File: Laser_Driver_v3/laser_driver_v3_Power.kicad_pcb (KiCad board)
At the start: 2 copper layers, 261.3 x 165.2 mm, 178 parts, among them J1 Screw_Terminal_01x03, J2 Screw_Terminal_01x03, J3 Screw_Terminal_01x03, J4 Screw_Terminal_01x03, J5 Screw_Terminal_01x03, J6 Conn_02x12_Counter_Clockwise, Q1 IRF540NPBF, Q10 Q_NPN MJL21194, Q2 IRF9540NPBF, Q3 IRF540NPBF, Q4 IRF9540NPBF, Q5 MMBT2907, Q6 MMBT2222, Q7 Q_PNP_MJL21193, Q8 Q_PNP_MJL21193, Q9 Q_NPN MJL21194, U1 MC7808CTG, U10 LT3042EMSE +14.3V, U11 LM4041A, U12 LM4041, U13 MC7812CTG, U14 MC7808CTG, U15 LT3045EMSE 5V, U16 LT3045EMSE 5V, U17 MC7808CTG, U18 LM7905_TO220, U19 LT3045EMSE 5V, U2 LT3042EMSE +5.5V, U20 LT3094EMSE -5V, U21 OPA192IDBVR, U3 LTC6655BHMS8-5#PBF, U4 MC7812CTG, U5 MC7805CTG, U6 LT3045EMSE 3.3V, U7 LP5907MFX-1.8, U8 TPS7A3901DSCR, U9 LT3094EMSE -14.3V

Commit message: Update zeners to LM4051 SOT-23
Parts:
- R25: moved to F.Cu
- U11: value LM4041A -> LM4051AIM3-ADJ/NOPB; footprint Package_TO_SOT_THT:TO-92_Inline -> Package_TO_SOT_SMD:SOT-23_Handsoldering
- U12: value LM4041 -> LM4051AIM3-ADJ/NOPB; footprint Package_TO_SOT_THT:TO-92_Inline -> Package_TO_SOT_SMD:SOT-23_Handsoldering
- moved R31 7.77 mm to (88.2, 109.8), turned to 0 degrees
- moved R30 4.62 mm to (85.2, 105.4), turned to -90 degrees
- moved R24 2.83 mm to (52.4, 109.2)
- moved R25 2.72 mm to (49.4, 106.0)
- moved U11 2.57 mm to (52.2, 105.5)
- moved U12 2.46 mm to (88.0, 105.9)
- moved C29 0.69 mm to (215.4, 52.0)
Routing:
- net DGND: track 498.0 -> 503.1 mm, vias 4 -> 3
- net Net-(U12-FB): track 7.51 -> 4.76 mm
- net Net-(D10-K): track 8.02 -> 5.46 mm
- net Net-(D11-A): track 7.88 -> 5.41 mm
- net Net-(U8-OUTN): track 60.1 -> 58.3 mm
- net Net-(U11-FB): track 5.89 -> 4.14 mm

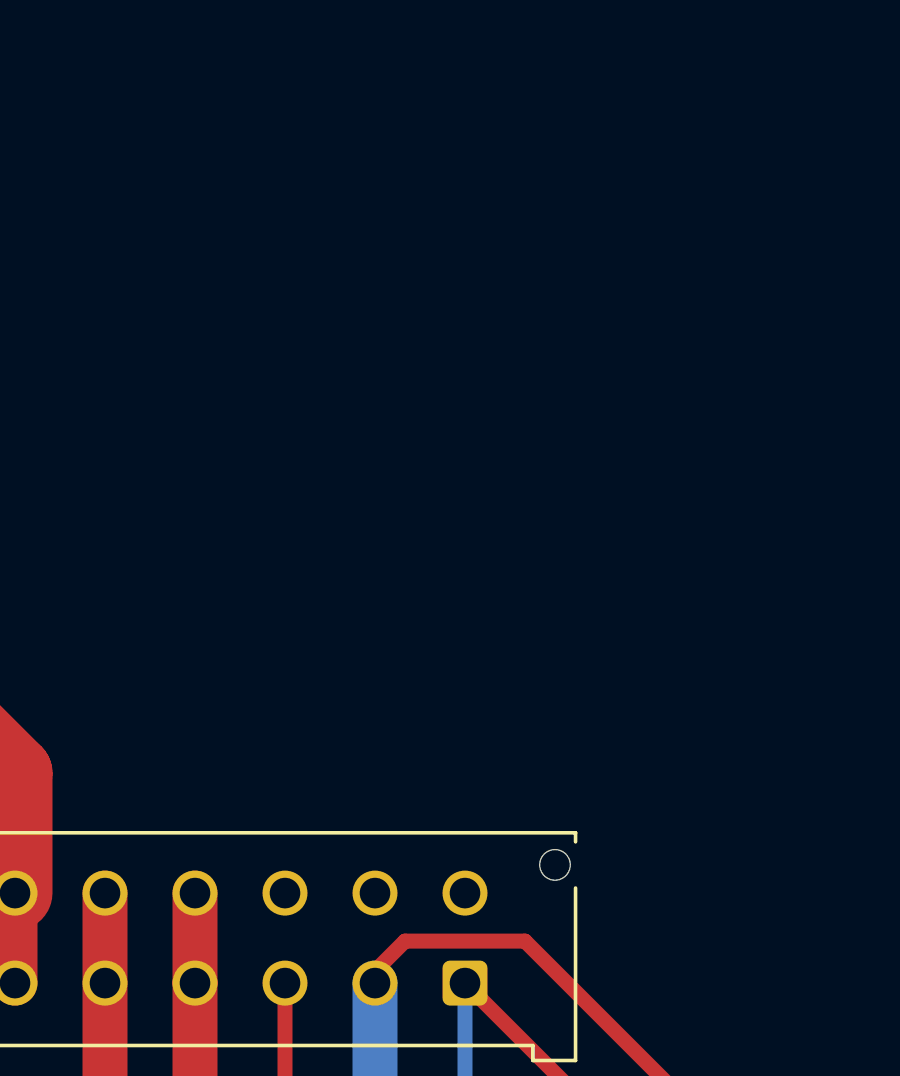
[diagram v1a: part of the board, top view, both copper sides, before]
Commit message: Added NTC for heatsink.  orrected screw terminal#s
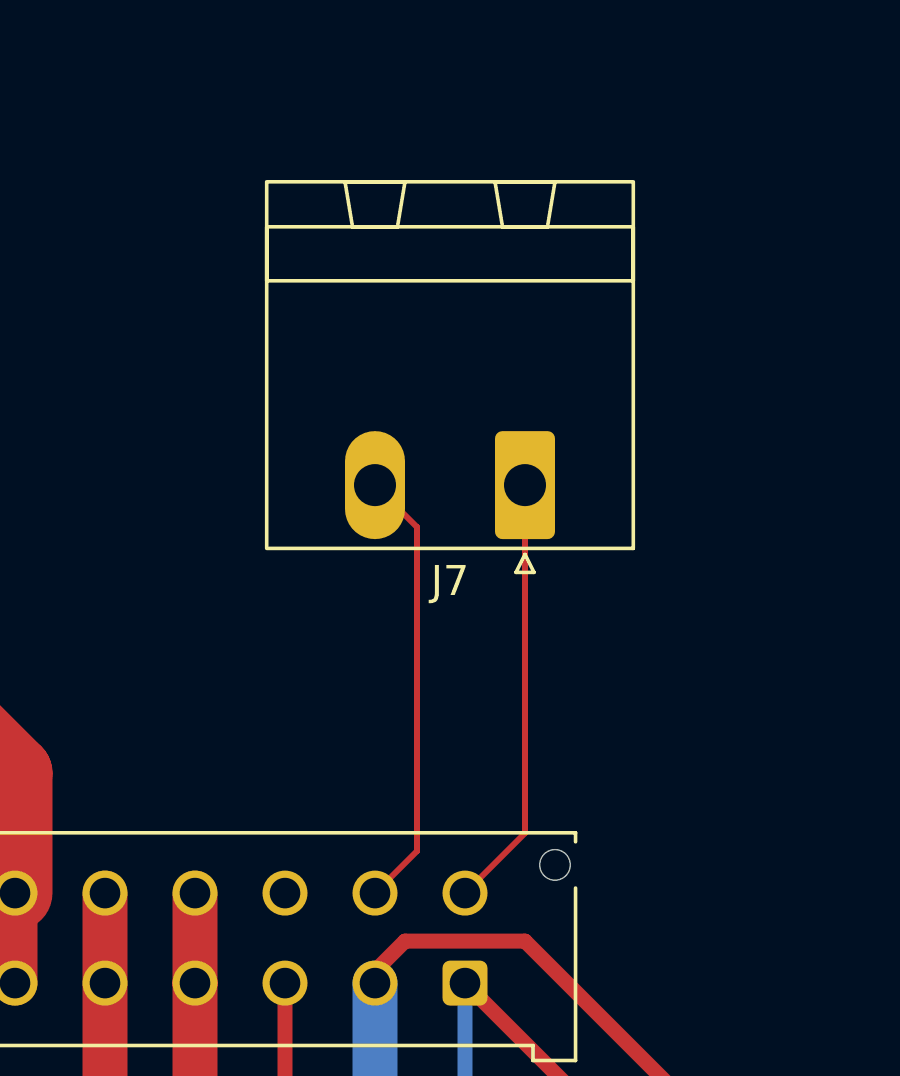
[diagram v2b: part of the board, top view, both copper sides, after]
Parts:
- added J7: Conn_01x02_Pin, Connector_Phoenix_MSTB:PhoenixContact_MSTBA_2,5_2-G_1x02_P5.00mm_Horizontal, F.Cu at (261.6, 33.8)
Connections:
- J6 pad 13: GND -> Net-(J6-Pin_13)
- J6 pad 14: GND -> Net-(J6-Pin_14)
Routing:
- net Net-(J6-Pin_14): track 0.00 -> 14.8 mm
- net Net-(J6-Pin_13): track 0.00 -> 14.4 mm

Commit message: Adding rail voltage good led circuitry.
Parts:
- added H1: MountingHole, MountingHole:MountingHole_3.2mm_M3, F.Cu at (22.6, 36.6)
- added H2: MountingHole, MountingHole:MountingHole_3.2mm_M3, F.Cu at (23.8, 170.4)
- added H3: MountingHole, MountingHole:MountingHole_3.2mm_M3, F.Cu at (142.6, 47.8)
- added H4: MountingHole, MountingHole:MountingHole_3.2mm_M3, F.Cu at (153.8, 121.0)
- added H5: MountingHole, MountingHole:MountingHole_3.2mm_M3, F.Cu at (271.0, 17.2)
- added H6: MountingHole, MountingHole:MountingHole_3.2mm_M3, F.Cu at (270.0, 170.4)
- added H7: GND, MountingHole:MountingHole_3.2mm_M3_DIN965_Pad_TopBottom, F.Cu at (108.0, 25.0)
- moved R3 14.1 mm to (183.0, 170.2)
- moved R20 14.1 mm to (79.1, 170.0)
- moved R2 14.1 mm to (234.6, 170.4)
- moved R21 14.1 mm to (130.2, 170.4)
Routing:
- net /Mains to +-18V/RAW22+: track 108.8 -> 126.7 mm
- net Net-(D8-K): track 188.8 -> 174.3 mm
- net Earth: track 14.1 -> 24.4 mm
- net /Mains to +-18V/-22VNF: track 172.8 -> 164.3 mm
- net /+-6V TEC/TEC_RAW+: track 233.1 -> 241.5 mm
- net /+-6V TEC/TEC_RAW-: track 313.9 -> 307.7 mm
- net /Mains to +-18V/RAW22-: track 103.1 -> 106.7 mm
- net Net-(J2-Pin_3): track 134.7 -> 132.0 mm
- net Net-(D9-A): track 141.9 -> 139.6 mm
- net /Mains to +-18V/+22VNF: track 136.4 -> 137.8 mm

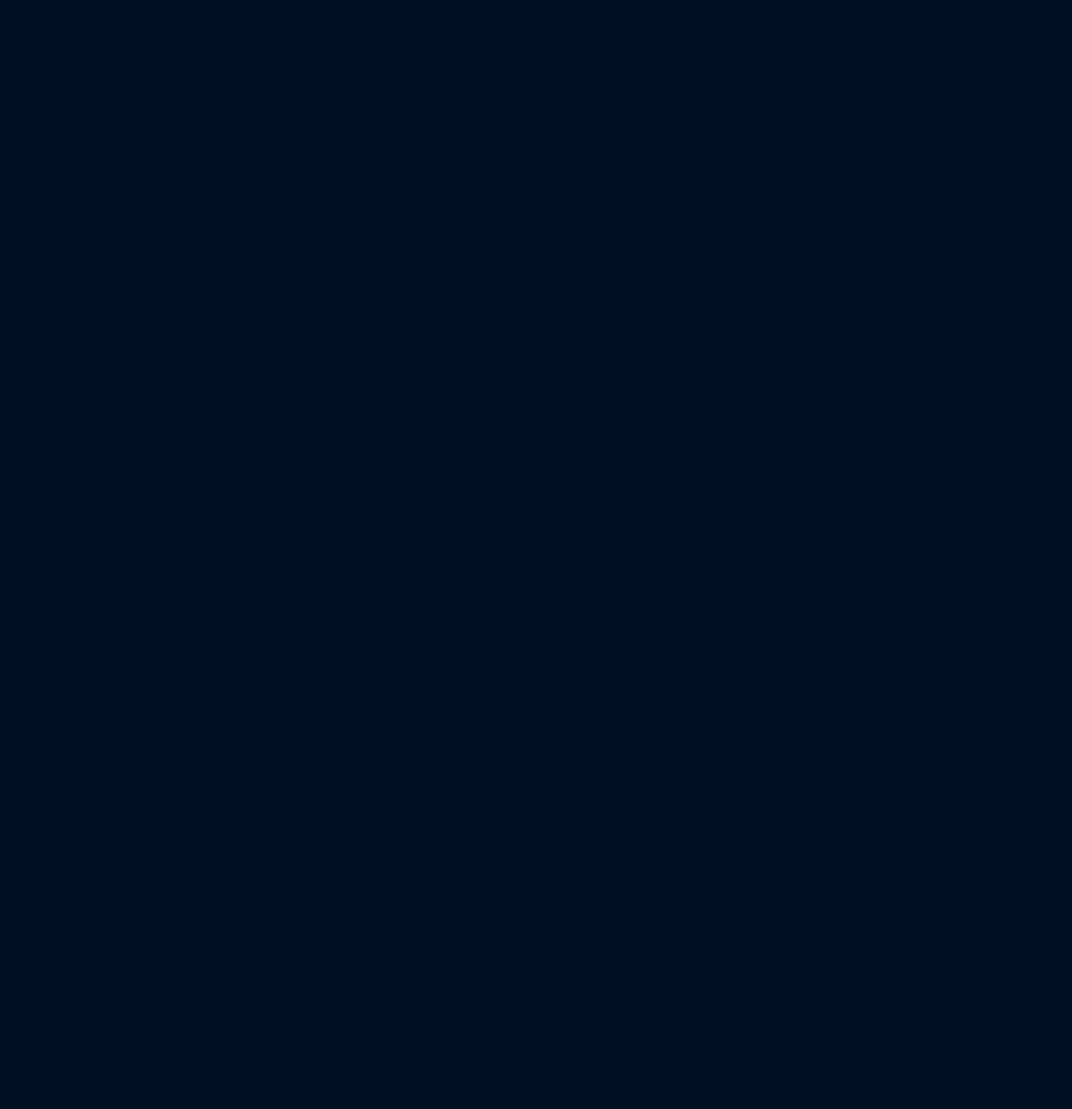
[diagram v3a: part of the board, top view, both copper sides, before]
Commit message: Started placing voltage monitor parts.
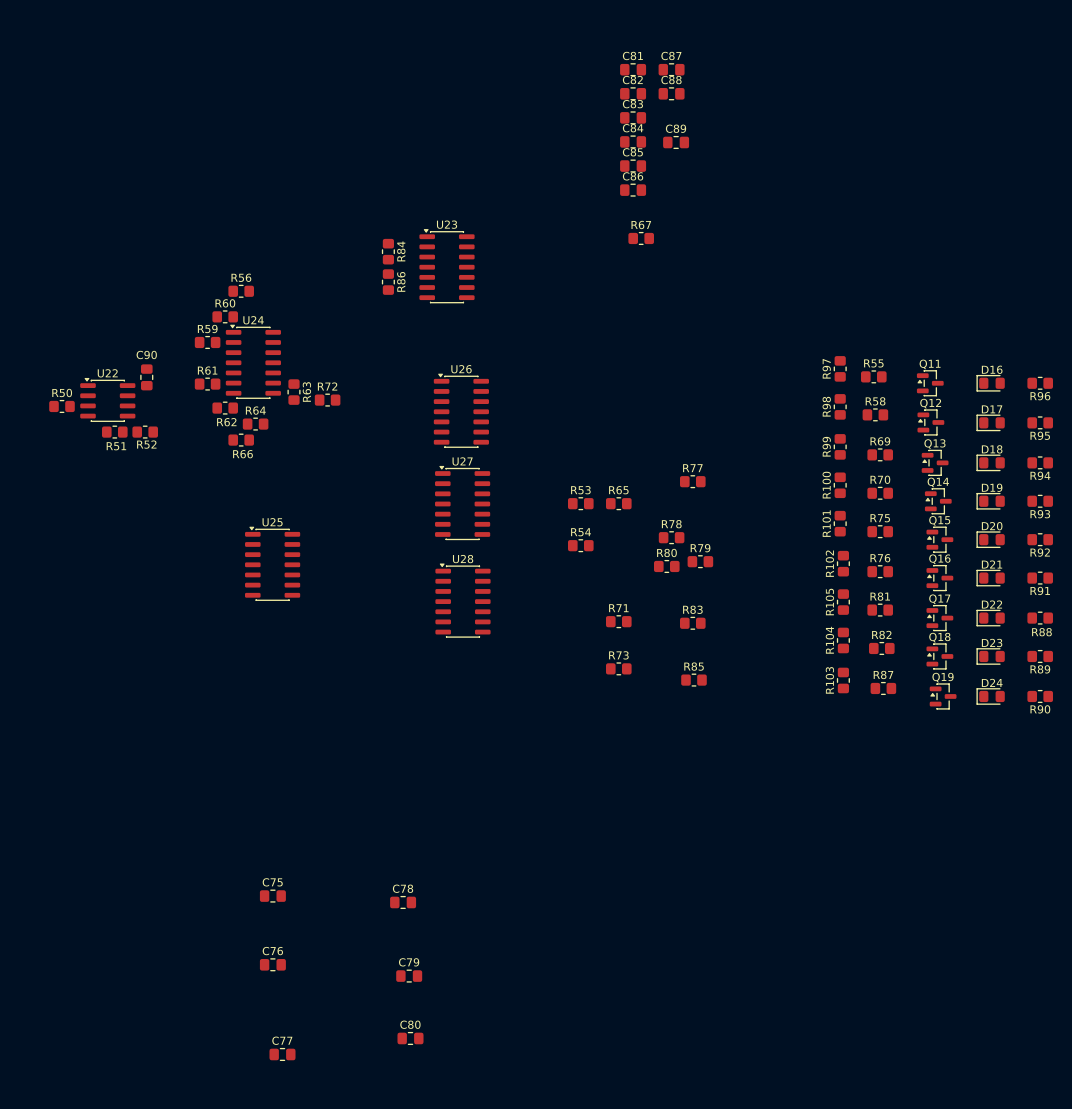
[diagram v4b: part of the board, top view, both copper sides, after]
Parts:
- added C75: 100nF, Capacitor_SMD:C_0805_2012Metric_Pad1.18x1.45mm_HandSolder, F.Cu at (311.6, 136.4)
- added C76: 100nF, Capacitor_SMD:C_0805_2012Metric_Pad1.18x1.45mm_HandSolder, F.Cu at (311.6, 145.0)
- added C77: 100nF, Capacitor_SMD:C_0805_2012Metric_Pad1.18x1.45mm_HandSolder, F.Cu at (312.8, 156.2)
- added C78: 100nF, Capacitor_SMD:C_0805_2012Metric_Pad1.18x1.45mm_HandSolder, F.Cu at (327.8, 137.2)
- added C79: 100nF, Capacitor_SMD:C_0805_2012Metric_Pad1.18x1.45mm_HandSolder, F.Cu at (328.6, 146.4)
- added C80: 100nF, Capacitor_SMD:C_0805_2012Metric_Pad1.18x1.45mm_HandSolder, F.Cu at (328.8, 154.2)
- added C81: 10nF, Capacitor_SMD:C_0805_2012Metric_Pad1.18x1.45mm_HandSolder, F.Cu at (356.6, 33.1)
- added C82: 10nF, Capacitor_SMD:C_0805_2012Metric_Pad1.18x1.45mm_HandSolder, F.Cu at (356.6, 36.1)
- added C83: 10nF, Capacitor_SMD:C_0805_2012Metric_Pad1.18x1.45mm_HandSolder, F.Cu at (356.6, 39.1)
- added C84: 10nF, Capacitor_SMD:C_0805_2012Metric_Pad1.18x1.45mm_HandSolder, F.Cu at (356.6, 42.1)
- added C85: 10nF, Capacitor_SMD:C_0805_2012Metric_Pad1.18x1.45mm_HandSolder, F.Cu at (356.6, 45.1)
- added C86: 10nF, Capacitor_SMD:C_0805_2012Metric_Pad1.18x1.45mm_HandSolder, F.Cu at (356.6, 48.2)
- added C87: 10nF, Capacitor_SMD:C_0805_2012Metric_Pad1.18x1.45mm_HandSolder, F.Cu at (361.4, 33.1)
- added C88: 10nF, Capacitor_SMD:C_0805_2012Metric_Pad1.18x1.45mm_HandSolder, F.Cu at (361.4, 36.1)
- added C89: 10nF, Capacitor_SMD:C_0805_2012Metric_Pad1.18x1.45mm_HandSolder, F.Cu at (362.0, 42.2)
- added C90: 100nF, Capacitor_SMD:C_0805_2012Metric_Pad1.18x1.45mm_HandSolder, F.Cu at (295.8, 71.6)
- added D16: +15V_OK, LED_SMD:LED_0805_2012Metric_Pad1.15x1.40mm_HandSolder, F.Cu at (401.4, 72.3)
- added D17: -15V_OK, LED_SMD:LED_0805_2012Metric_Pad1.15x1.40mm_HandSolder, F.Cu at (401.4, 77.2)
- added D18: +5V_OK, LED_SMD:LED_0805_2012Metric_Pad1.15x1.40mm_HandSolder, F.Cu at (401.4, 82.2)
- added D19: -5V_OK, LED_SMD:LED_0805_2012Metric_Pad1.15x1.40mm_HandSolder, F.Cu at (401.4, 87.0)
- added D20: +6V_OK, LED_SMD:LED_0805_2012Metric_Pad1.15x1.40mm_HandSolder, F.Cu at (401.4, 91.8)
- added D21: -6V_OK, LED_SMD:LED_0805_2012Metric_Pad1.15x1.40mm_HandSolder, F.Cu at (401.4, 96.7)
- added D22: +5VLaser_OK, LED_SMD:LED_0805_2012Metric_Pad1.15x1.40mm_HandSolder, F.Cu at (401.4, 101.7)
- added D23: 3V3_OK, LED_SMD:LED_0805_2012Metric_Pad1.15x1.40mm_HandSolder, F.Cu at (401.4, 106.5)
- added D24: 1V8_OK, LED_SMD:LED_0805_2012Metric_Pad1.15x1.40mm_HandSolder, F.Cu at (401.4, 111.5)
- added Q11: MMBT3904, Package_TO_SOT_SMD:SOT-23, F.Cu at (393.7, 72.3)
- added Q12: MMBT3904, Package_TO_SOT_SMD:SOT-23, F.Cu at (393.8, 77.2)
- added Q13: MMBT3904, Package_TO_SOT_SMD:SOT-23, F.Cu at (394.3, 82.2)
- added Q14: MMBT3904, Package_TO_SOT_SMD:SOT-23, F.Cu at (394.7, 87.0)
- added Q15: MMBT3904, Package_TO_SOT_SMD:SOT-23, F.Cu at (394.9, 91.8)
- added Q16: MMBT3904, Package_TO_SOT_SMD:SOT-23, F.Cu at (394.9, 96.7)
- added Q17: MMBT3904, Package_TO_SOT_SMD:SOT-23, F.Cu at (394.9, 101.7)
- added Q18: MMBT3904, Package_TO_SOT_SMD:SOT-23, F.Cu at (394.9, 106.5)
- added Q19: MMBT3904, Package_TO_SOT_SMD:SOT-23, F.Cu at (395.3, 111.5)
- added R100: 4.7k, Resistor_SMD:R_0805_2012Metric_Pad1.20x1.40mm_HandSolder, F.Cu at (382.5, 85.0)
- added R101: 4.7k, Resistor_SMD:R_0805_2012Metric_Pad1.20x1.40mm_HandSolder, F.Cu at (382.5, 89.8)
- added R102: 4.7k, Resistor_SMD:R_0805_2012Metric_Pad1.20x1.40mm_HandSolder, F.Cu at (382.9, 94.8)
- added R103: 4.7k, Resistor_SMD:R_0805_2012Metric_Pad1.20x1.40mm_HandSolder, F.Cu at (382.9, 109.5)
- added R104: 4.7k, Resistor_SMD:R_0805_2012Metric_Pad1.20x1.40mm_HandSolder, F.Cu at (382.9, 104.5)
- added R105: 4.7k, Resistor_SMD:R_0805_2012Metric_Pad1.20x1.40mm_HandSolder, F.Cu at (382.9, 99.7)
- added R50: 29.4k, Resistor_SMD:R_0805_2012Metric_Pad1.20x1.40mm_HandSolder, F.Cu at (285.2, 75.2)
- added R51: 1k, Resistor_SMD:R_0805_2012Metric_Pad1.20x1.40mm_HandSolder, F.Cu at (291.8, 78.4)
- added R52: 9.53k, Resistor_SMD:R_0805_2012Metric_Pad1.20x1.40mm_HandSolder, F.Cu at (295.6, 78.4)
- added R53: 110k, Resistor_SMD:R_0805_2012Metric_Pad1.20x1.40mm_HandSolder, F.Cu at (350.1, 87.3)
- added R54: 10k, Resistor_SMD:R_0805_2012Metric_Pad1.20x1.40mm_HandSolder, F.Cu at (350.1, 92.6)
- added R55: 10k, Resistor_SMD:R_0805_2012Metric_Pad1.20x1.40mm_HandSolder, F.Cu at (386.7, 71.5)
- added R56: 100, Resistor_SMD:R_0805_2012Metric_Pad1.20x1.40mm_HandSolder, F.Cu at (307.6, 60.8)
- added R58: 10k, Resistor_SMD:R_0805_2012Metric_Pad1.20x1.40mm_HandSolder, F.Cu at (386.9, 76.2)
- added R59: 120k, Resistor_SMD:R_0805_2012Metric_Pad1.20x1.40mm_HandSolder, F.Cu at (303.4, 67.2)
- added R60: 10k, Resistor_SMD:R_0805_2012Metric_Pad1.20x1.40mm_HandSolder, F.Cu at (305.6, 64.0)
- added R61: 40.2k, Resistor_SMD:R_0805_2012Metric_Pad1.20x1.40mm_HandSolder, F.Cu at (303.4, 72.4)
- added R62: 10k, Resistor_SMD:R_0805_2012Metric_Pad1.20x1.40mm_HandSolder, F.Cu at (305.6, 75.4)
- added R63: 10k, Resistor_SMD:R_0805_2012Metric_Pad1.20x1.40mm_HandSolder, F.Cu at (314.2, 73.4)
- added R64: 47.5k, Resistor_SMD:R_0805_2012Metric_Pad1.20x1.40mm_HandSolder, F.Cu at (309.4, 77.4)
- added R65: 30.1k, Resistor_SMD:R_0805_2012Metric_Pad1.20x1.40mm_HandSolder, F.Cu at (354.8, 87.3)
- added R66: 100, Resistor_SMD:R_0805_2012Metric_Pad1.20x1.40mm_HandSolder, F.Cu at (307.6, 79.4)
- added R67: 10k, Resistor_SMD:R_0805_2012Metric_Pad1.20x1.40mm_HandSolder, F.Cu at (357.6, 54.2)
- added R69: 10k, Resistor_SMD:R_0805_2012Metric_Pad1.20x1.40mm_HandSolder, F.Cu at (387.5, 81.2)
- added R70: 10k, Resistor_SMD:R_0805_2012Metric_Pad1.20x1.40mm_HandSolder, F.Cu at (387.5, 86.0)
- added R71: 38.3k, Resistor_SMD:R_0805_2012Metric_Pad1.20x1.40mm_HandSolder, F.Cu at (354.8, 102.1)
- added R72: 100, Resistor_SMD:R_0805_2012Metric_Pad1.20x1.40mm_HandSolder, F.Cu at (318.4, 74.4)
- added R73: 10k, Resistor_SMD:R_0805_2012Metric_Pad1.20x1.40mm_HandSolder, F.Cu at (354.8, 108.0)
- added R75: 10k, Resistor_SMD:R_0805_2012Metric_Pad1.20x1.40mm_HandSolder, F.Cu at (387.5, 90.8)
- added R76: 10k, Resistor_SMD:R_0805_2012Metric_Pad1.20x1.40mm_HandSolder, F.Cu at (387.5, 95.8)
- added R77: 30.1k, Resistor_SMD:R_0805_2012Metric_Pad1.20x1.40mm_HandSolder, F.Cu at (364.1, 84.6)
- added R78: 16.5k, Resistor_SMD:R_0805_2012Metric_Pad1.20x1.40mm_HandSolder, F.Cu at (361.4, 91.6)
- added R79: 10k, Resistor_SMD:R_0805_2012Metric_Pad1.20x1.40mm_HandSolder, F.Cu at (365.0, 94.6)
- added R80: 10k, Resistor_SMD:R_0805_2012Metric_Pad1.20x1.40mm_HandSolder, F.Cu at (360.8, 95.2)
- added R81: 10k, Resistor_SMD:R_0805_2012Metric_Pad1.20x1.40mm_HandSolder, F.Cu at (387.5, 100.7)
- added R82: 10k, Resistor_SMD:R_0805_2012Metric_Pad1.20x1.40mm_HandSolder, F.Cu at (387.7, 105.5)
- added R83: 4.42k, Resistor_SMD:R_0805_2012Metric_Pad1.20x1.40mm_HandSolder, F.Cu at (364.1, 102.3)
- added R84: 10k, Resistor_SMD:R_0805_2012Metric_Pad1.20x1.40mm_HandSolder, F.Cu at (326.0, 55.9)
- added R85: 10k, Resistor_SMD:R_0805_2012Metric_Pad1.20x1.40mm_HandSolder, F.Cu at (364.2, 109.4)
- added R86: 10k, Resistor_SMD:R_0805_2012Metric_Pad1.20x1.40mm_HandSolder, F.Cu at (326.0, 59.6)
- added R87: 10k, Resistor_SMD:R_0805_2012Metric_Pad1.20x1.40mm_HandSolder, F.Cu at (387.9, 110.5)
- added R88: 1.3k, Resistor_SMD:R_0805_2012Metric_Pad1.20x1.40mm_HandSolder, F.Cu at (407.5, 101.7)
- added R89: 1.3k, Resistor_SMD:R_0805_2012Metric_Pad1.20x1.40mm_HandSolder, F.Cu at (407.5, 106.5)
- added R90: 1.3k, Resistor_SMD:R_0805_2012Metric_Pad1.20x1.40mm_HandSolder, F.Cu at (407.5, 111.5)
- added R91: 1.3k, Resistor_SMD:R_0805_2012Metric_Pad1.20x1.40mm_HandSolder, F.Cu at (407.5, 96.7)
- added R92: 1.3k, Resistor_SMD:R_0805_2012Metric_Pad1.20x1.40mm_HandSolder, F.Cu at (407.5, 91.8)
- added R93: 1.3k, Resistor_SMD:R_0805_2012Metric_Pad1.20x1.40mm_HandSolder, F.Cu at (407.5, 87.0)
- added R94: 1.3k, Resistor_SMD:R_0805_2012Metric_Pad1.20x1.40mm_HandSolder, F.Cu at (407.5, 82.2)
- added R95: 1.3k, Resistor_SMD:R_0805_2012Metric_Pad1.20x1.40mm_HandSolder, F.Cu at (407.5, 77.2)
- added R96: 1.3k, Resistor_SMD:R_0805_2012Metric_Pad1.20x1.40mm_HandSolder, F.Cu at (407.5, 72.3)
- added R97: 4.7k, Resistor_SMD:R_0805_2012Metric_Pad1.20x1.40mm_HandSolder, F.Cu at (382.5, 70.5)
- added R98: 4.7k, Resistor_SMD:R_0805_2012Metric_Pad1.20x1.40mm_HandSolder, F.Cu at (382.5, 75.2)
- added R99: 4.7k, Resistor_SMD:R_0805_2012Metric_Pad1.20x1.40mm_HandSolder, F.Cu at (382.5, 80.2)
- added U22: MCP6002-xMC, Package_SO:SOIC-8_3.9x4.9mm_P1.27mm, F.Cu at (290.9, 74.5)
- added U23: LM339, Package_SO:SOIC-14_3.9x8.7mm_P1.27mm, F.Cu at (333.3, 57.8)
- added U24: MCP6004, Package_SO:SOIC-14_3.9x8.7mm_P1.27mm, F.Cu at (309.1, 69.7)
- added U25: LM339, Package_SO:SOIC-14_3.9x8.7mm_P1.27mm, F.Cu at (311.5, 95.0)
- added U26: LM339, Package_SO:SOIC-14_3.9x8.7mm_P1.27mm, F.Cu at (335.1, 75.9)
- added U27: LM339, Package_SO:SOIC-14_3.9x8.7mm_P1.27mm, F.Cu at (335.3, 87.4)
- added U28: LM339, Package_SO:SOIC-14_3.9x8.7mm_P1.27mm, F.Cu at (335.3, 99.6)
